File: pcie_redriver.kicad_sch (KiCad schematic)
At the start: 75 parts, among them U39 PI3EQX16904GL, U40 PI3EQX16904GL

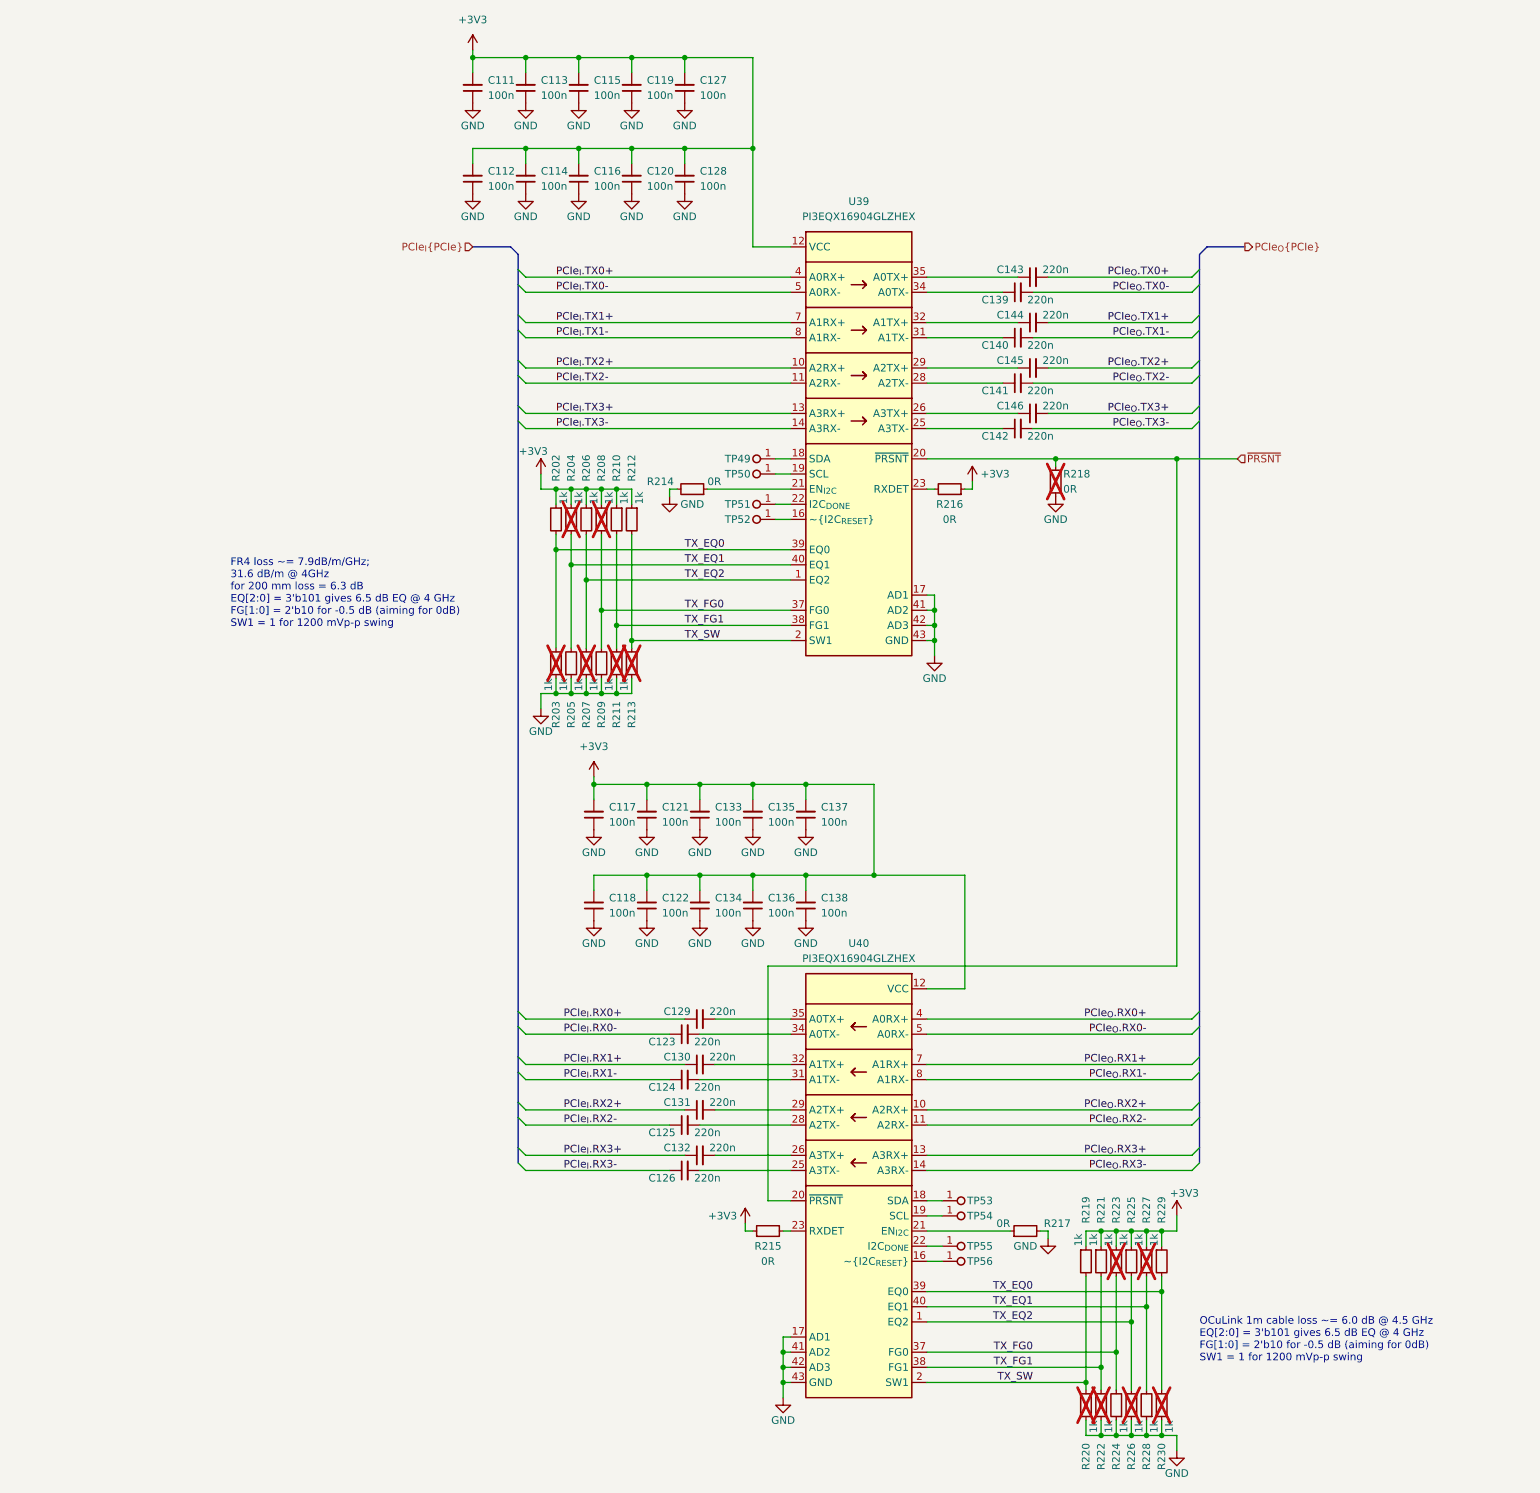
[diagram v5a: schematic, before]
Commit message: [#65447] Fix rotated LEDs, overlapping text and symbols, add rules
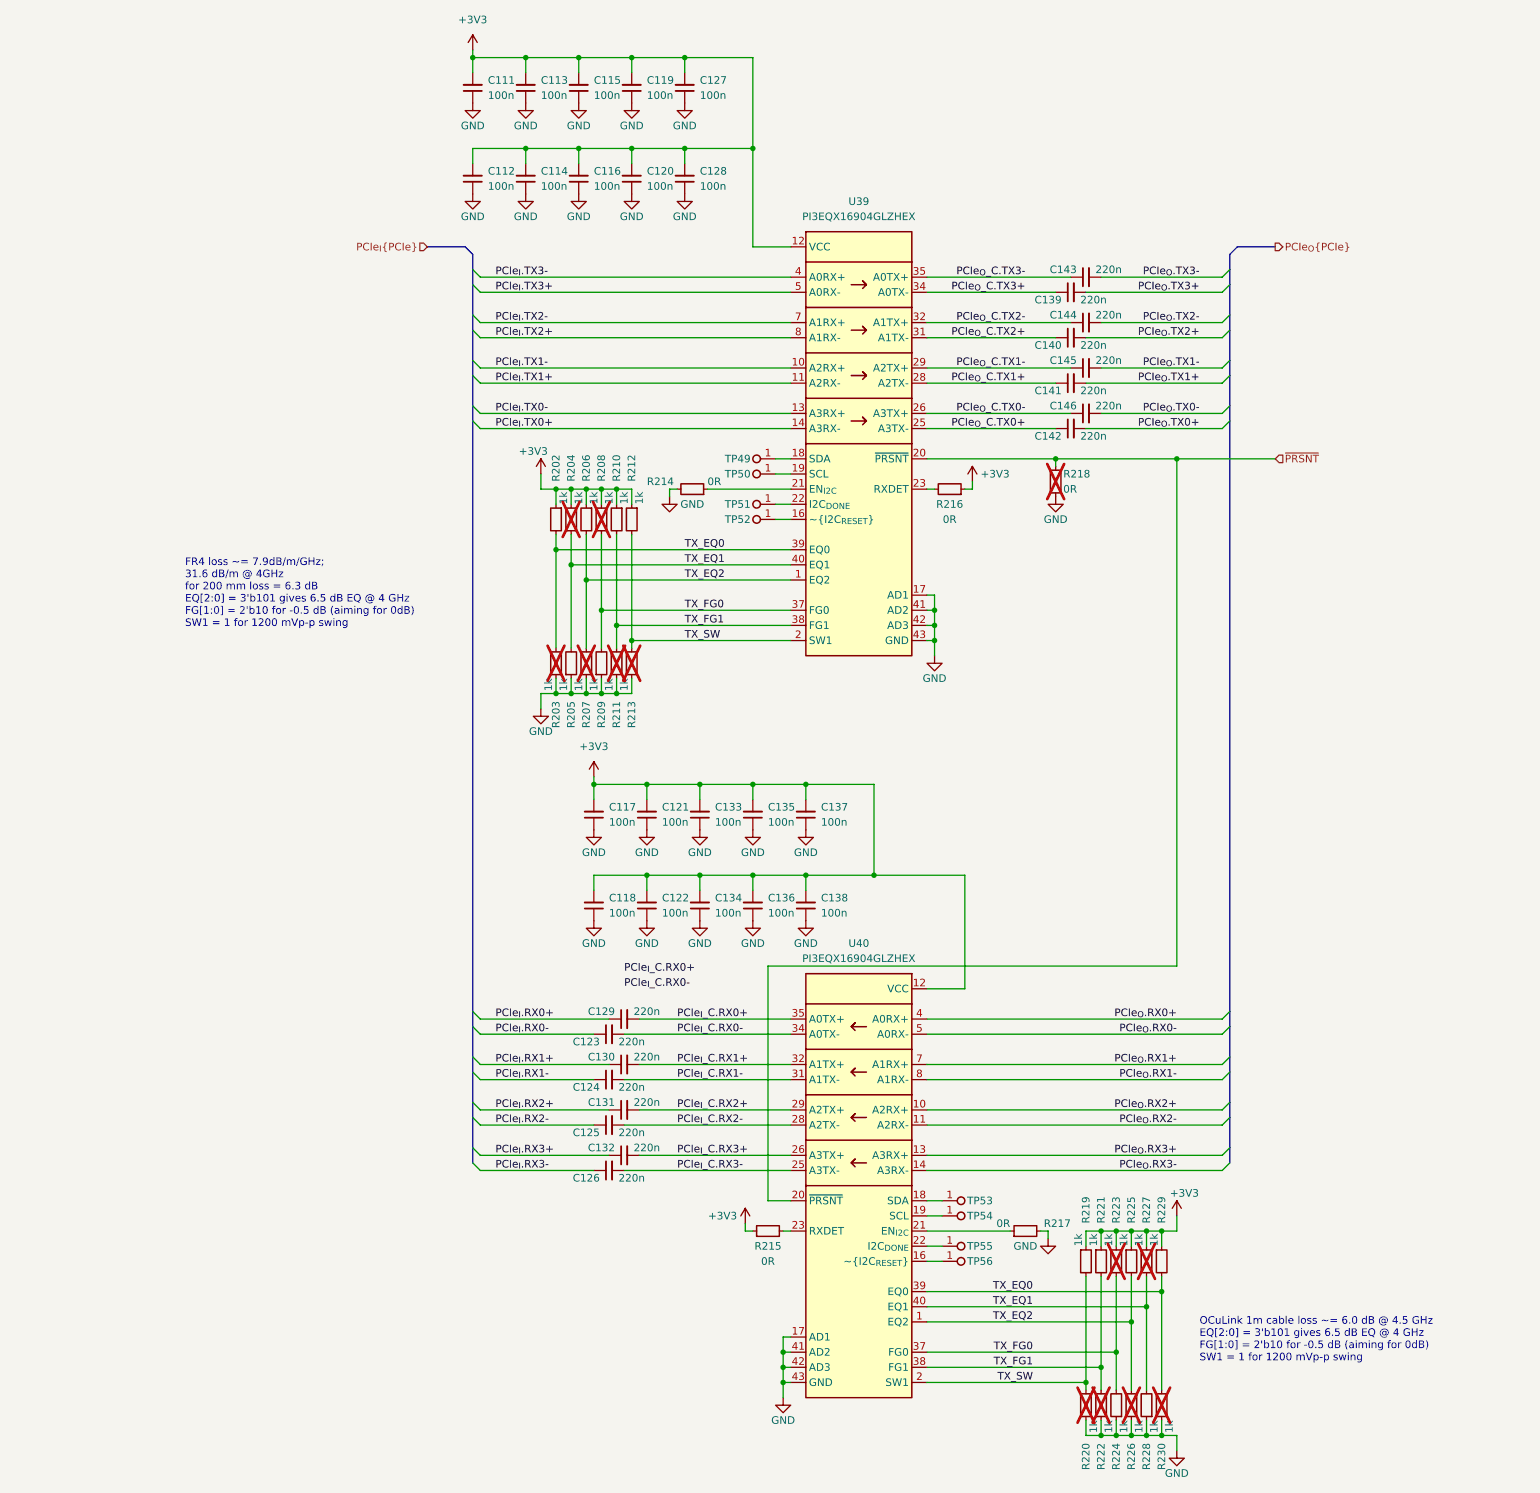
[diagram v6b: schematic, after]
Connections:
- net PCIe_{I}.TX0+: now also U39.14 (A3RX-); no longer U39.4 (A0RX+)
- net PCIe_{I}.TX0-: now also U39.13 (A3RX+); no longer U39.5 (A0RX-)
- net PCIe_{I}.TX1+: now also U39.11 (A2RX-); no longer U39.7 (A1RX+)
- net PCIe_{I}.TX1-: now also U39.10 (A2RX+); no longer U39.8 (A1RX-)
- net PCIe_{I}.TX2+: now also U39.8 (A1RX-); no longer U39.10 (A2RX+)
- net PCIe_{I}.TX2-: now also U39.7 (A1RX+); no longer U39.11 (A2RX-)
- net PCIe_{I}.TX3+: now also U39.5 (A0RX-); no longer U39.13 (A3RX+)
- net PCIe_{I}.TX3-: now also U39.4 (A0RX+); no longer U39.14 (A3RX-)
- net PCIe_{O}.TX0+: now also C142.2; no longer C143.2
- net PCIe_{O}.TX0-: now also C146.2; no longer C139.2
- net PCIe_{O}.TX1+: now also C141.2; no longer C144.2
- net PCIe_{O}.TX1-: now also C145.2; no longer C140.2
- net PCIe_{O}.TX2+: now also C140.2; no longer C145.2
- net PCIe_{O}.TX2-: now also C144.2; no longer C141.2
- net PCIe_{O}.TX3+: now also C139.2; no longer C146.2
- net PCIe_{O}.TX3-: now also C143.2; no longer C142.2
- net PCIe_{O}_C.TX1+: now reaches C141.1, U39.28 (A2TX-)
- net PCIe_{O}_C.TX2-: now reaches C144.1, U39.32 (A1TX+)
- net PCIe_{O}_C.TX0-: now reaches C146.1, U39.26 (A3TX+)
- net PCIe_{O}_C.TX3+: now reaches C139.1, U39.34 (A0TX-)
- net PCIe_{I}_C.RX3-: now reaches C126.2, U40.25 (A3TX-)
- net PCIe_{O}_C.TX2+: now reaches C140.1, U39.31 (A1TX-)
- net PCIe_{O}_C.TX0+: now reaches C142.1, U39.25 (A3TX-)
- net PCIe_{O}_C.TX3-: now reaches C143.1, U39.35 (A0TX+)
- net PCIe_{I}_C.RX3+: now reaches C132.2, U40.26 (A3TX+)
- net PCIe_{I}_C.RX2-: now reaches C125.2, U40.28 (A2TX-)
- net PCIe_{I}_C.RX2+: now reaches C131.2, U40.29 (A2TX+)
- net PCIe_{I}_C.RX1-: now reaches C124.2, U40.31 (A1TX-)
- net PCIe_{I}_C.RX1+: now reaches C130.2, U40.32 (A1TX+)
- net PCIe_{I}_C.RX0-: now reaches C123.2, U40.34 (A0TX-)
- net PCIe_{I}_C.RX0+: now reaches C129.2, U40.35 (A0TX+)
- net PCIe_{O}_C.TX1-: now reaches C145.1, U39.29 (A2TX+)
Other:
- moved on the sheet: C123, C124, C125, C126, C129, C130, C131, C132, C139, C140, C141, C142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

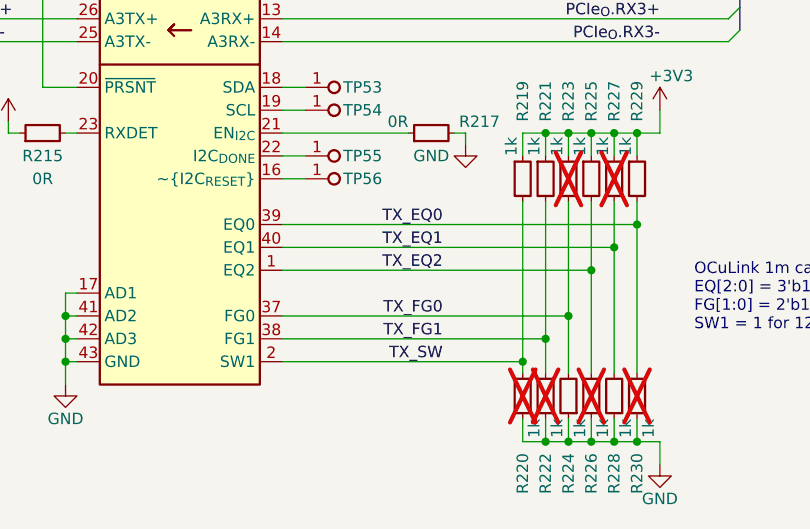
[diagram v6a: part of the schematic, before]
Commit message: [#66613] Split EQ, FG and SW lines of PCIe redrivers, align PCIe, misc signals
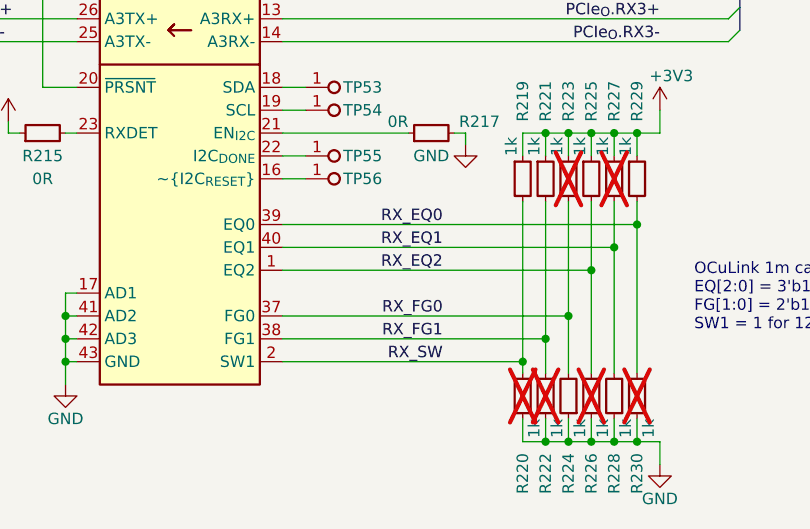
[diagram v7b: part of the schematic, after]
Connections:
- net TX_EQ0: no longer R229.2, R230.2, U40.39 (EQ0)
- net TX_EQ1: no longer R227.2, R228.2, U40.40 (EQ1)
- net TX_EQ2: no longer R225.2, R226.2, U40.1 (EQ2)
- net TX_FG0: no longer R223.2, R224.2, U40.37 (FG0)
- net TX_FG1: no longer R221.2, R222.2, U40.38 (FG1)
- net TX_SW: no longer R219.2, R220.2, U40.2 (SW1)
- new net RX_EQ0: R229.2, R230.2, U40.39 (EQ0)
- new net RX_EQ1: R227.2, R228.2, U40.40 (EQ1)
- new net RX_EQ2: R225.2, R226.2, U40.1 (EQ2)
- new net RX_FG0: R223.2, R224.2, U40.37 (FG0)
- new net RX_FG1: R221.2, R222.2, U40.38 (FG1)
- new net RX_SW: R219.2, R220.2, U40.2 (SW1)
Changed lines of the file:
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@@
     (effects (font (size 1.27 1.27)) (justify left bottom))
   )
-  (label "TX_EQ0" (at 226.06 229.87 180) (fields_autoplaced)
+  (label "RX_EQ0" (at 226.06 229.87 180) (fields_autoplaced)
     (effects (font (size 1.27 1.27)) (justify right bottom))
   )
@@
     (effects (font (size 1.27 1.27)) (justify right bottom))
   )
-  (label "TX_FG1" (at 226.06 242.57 180) (fields_autoplaced)
+  (label "RX_FG1" (at 226.06 242.57 180) (fields_autoplaced)
     (effects (font (size 1.27 1.27)) (justify right bottom))
   )
@@
     (effects (font (size 1.27 1.27)) (justify left bottom))
   )
-  (label "TX_FG0" (at 226.06 240.03 180) (fields_autoplaced)
+  (label "RX_FG0" (at 226.06 240.03 180) (fields_autoplaced)
     (effects (font (size 1.27 1.27)) (justify right bottom))
   )
@@
     (effects (font (size 1.27 1.27)) (justify right bottom))
   )
-  (label "TX_EQ2" (at 226.06 234.95 180) (fields_autoplaced)
+  (label "RX_EQ2" (at 226.06 234.95 180) (fields_autoplaced)
     (effects (font (size 1.27 1.27)) (justify right bottom))
   )
@@
     (effects (font (size 1.27 1.27)) (justify right bottom))
   )
-  (label "TX_EQ1" (at 226.06 232.41 180) (fields_autoplaced)
+  (label "RX_EQ1" (at 226.06 232.41 180) (fields_autoplaced)
     (effects (font (size 1.27 1.27)) (justify right bottom))
   )
@@
     (effects (font (size 1.27 1.27)) (justify left bottom))
   )
-  (label "TX_SW" (at 226.06 245.11 180) (fields_autoplaced)
+  (label "RX_SW" (at 226.06 245.11 180) (fields_autoplaced)
     (effects (font (size 1.27 1.27)) (justify right bottom))
   )

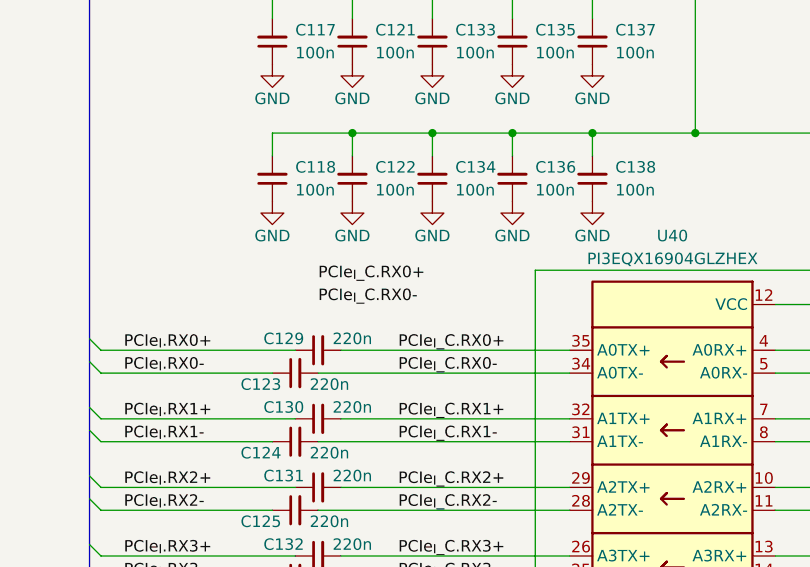
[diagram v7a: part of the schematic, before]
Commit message: [#66613] Fix ERC, adjust overlapping text on schematic
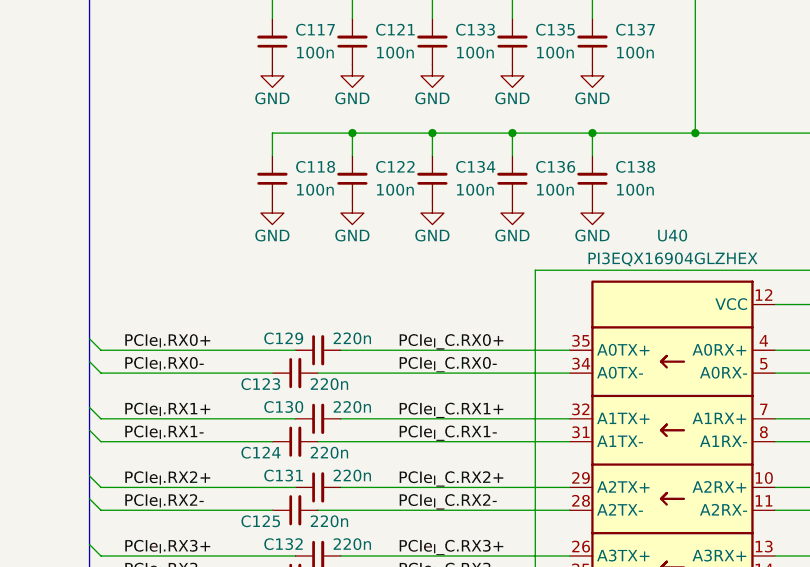
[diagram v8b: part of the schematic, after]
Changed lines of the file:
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@@
     (effects (font (size 1.27 1.27)) (justify right bottom))
-  )
-  (label "PCIe_{I}_C.RX0-" (at 157.48 179.07 0) (fields_autoplaced)
-    (effects (font (size 1.27 1.27)) (justify left bottom))
   )
   (label "PCIe_{I}_C.RX2+" (at 166.37 199.39 0) (fields_autoplaced)
@@
     (effects (font (size 1.27 1.27)) (justify left bottom))
   )
-  (label "PCIe_{I}_C.RX0+" (at 157.48 176.53 0) (fields_autoplaced)
-    (effects (font (size 1.27 1.27)) (justify left bottom))
-  )
